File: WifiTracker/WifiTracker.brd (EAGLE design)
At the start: 86.3 x 44.1 mm, 23 parts, among them Y1 16MHz

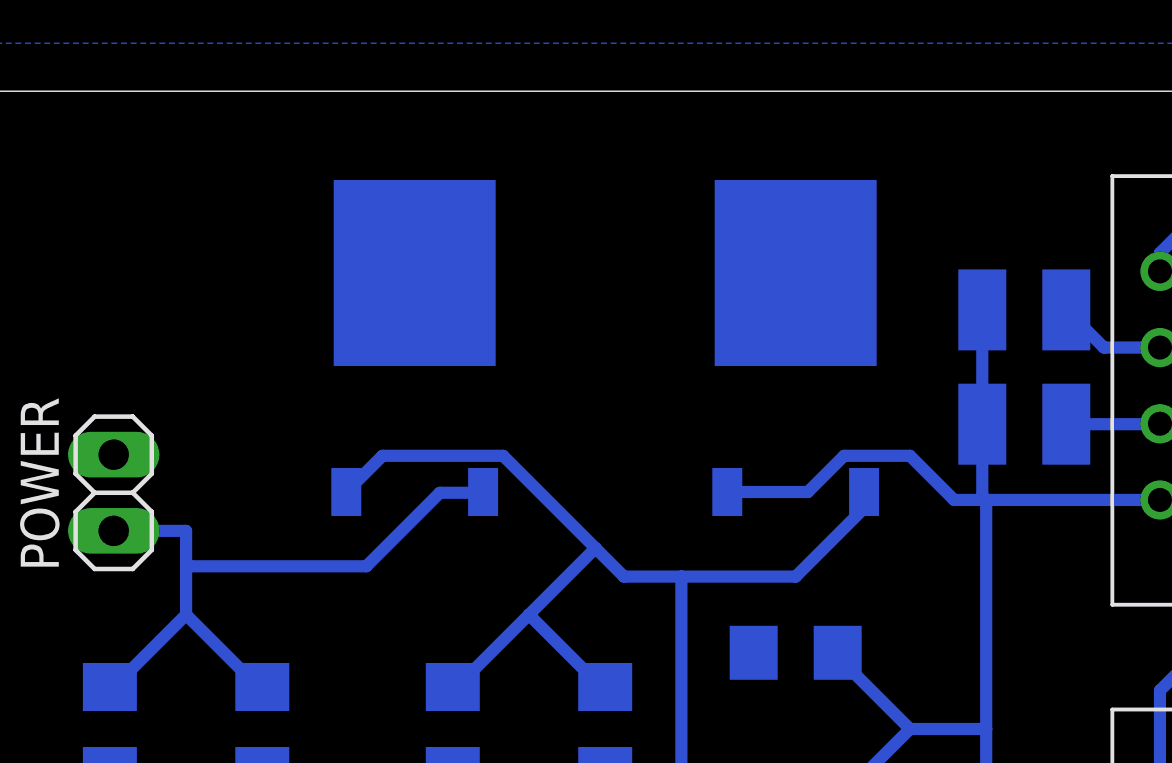
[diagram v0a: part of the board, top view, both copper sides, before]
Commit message: Change generic voltage regulator with specific one
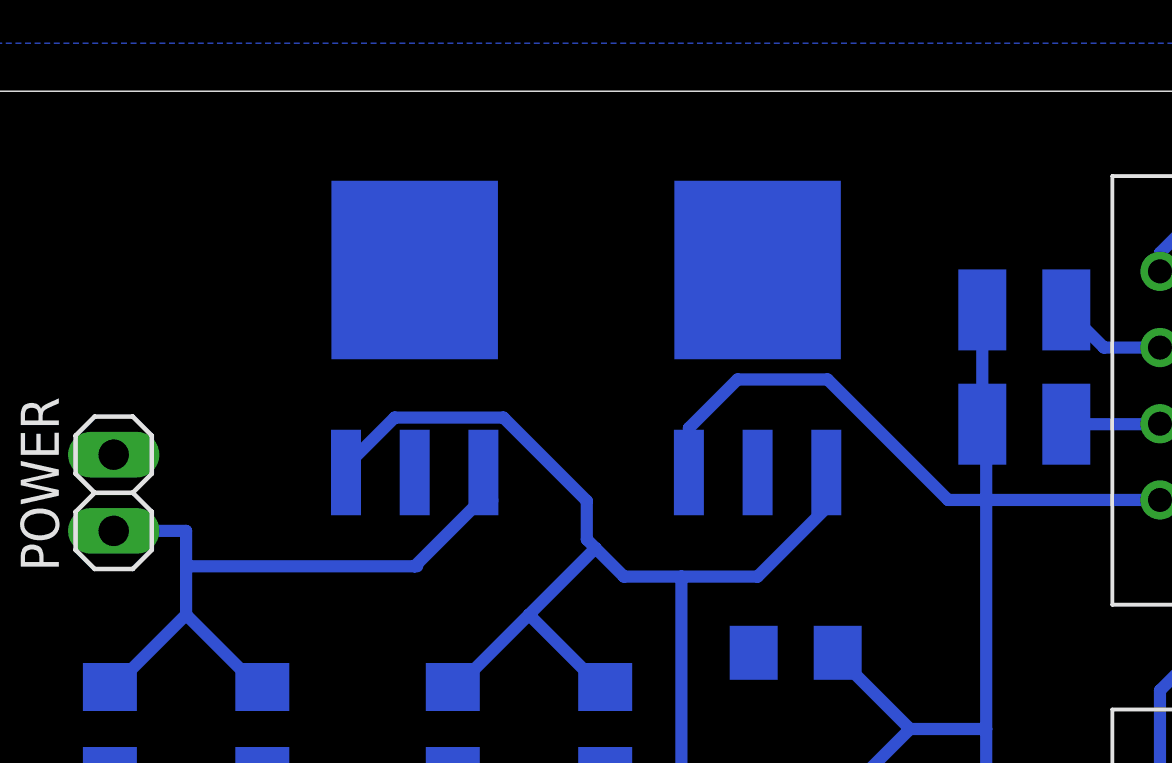
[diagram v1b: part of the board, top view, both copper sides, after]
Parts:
- 3V_REG, 5V_REG: value 7808DT -> LP2950CDT-5.0G; device linear:TO252 -> LP2950CDT-5.0G:TO229P990X238-4N
- moved 3V_REG 1.27 mm to (26.7, 35.6), turned to 90 degrees
- turned 5V_REG to 90 degrees
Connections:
- net 3VCC: now also 3V_REG.3; no longer 3V_REG.2
- net 5VCC: now also 5V_REG.3; no longer 5V_REG.2
- net GND: now also 3V_REG.2, 3V_REG.4, 5V_REG.2, 5V_REG.4; no longer 3V_REG.3, 5V_REG.3
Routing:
- net 3VCC: track 58.5 -> 62.5 mm
- net 5VCC: track 131.6 -> 132.6 mm

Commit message: fix
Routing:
- net 5VCC: track 132.6 -> 135.2 mm
- net VIN: track 23.4 -> 25.9 mm
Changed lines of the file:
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@@
 <wire x1="77.2892" y1="6.4008" x2="77.34" y2="6.35" width="0.4064" layer="16"/>
 <contactref element="5V_REG" pad="3"/>
-<wire x1="18.1983375" y1="33.2414" x2="20.9764" y2="30.4633375" width="0.4064" layer="16"/>
-<wire x1="20.9764" y1="30.4633375" x2="20.9764" y2="29.1783375" width="0.4064" layer="16"/>
-<wire x1="18.1983375" y1="33.2414" x2="14.5716625" y2="33.2414" width="0.4064" layer="16"/>
+<wire x1="18.1983375" y1="34.5114" x2="20.9764" y2="31.7333375" width="0.4064" layer="16"/>
+<wire x1="20.9764" y1="31.7333375" x2="20.9764" y2="29.1783375" width="0.4064" layer="16"/>
+<wire x1="18.1983375" y1="34.5114" x2="14.5716625" y2="34.5114" width="0.4064" layer="16"/>
 <wire x1="20.9764" y1="29.1783375" x2="21.26736875" y2="28.88736875" width="0.4064" layer="16"/>
-<wire x1="14.5716625" y1="33.2414" x2="12.95" y2="31.6197375" width="0.4064" layer="16"/>
-<wire x1="12.95" y1="31.6197375" x2="12.95" y2="31.41" width="0.4064" layer="16"/>
+<wire x1="14.5716625" y1="34.5114" x2="12.95" y2="32.8897375" width="0.4064" layer="16"/>
+<wire x1="12.95" y1="32.8897375" x2="12.95" y2="31.41" width="0.4064" layer="16"/>
 <contactref element="3V_REG" pad="1"/>
 <wire x1="28.96" y1="31.41" x2="28.96" y2="30.23" width="0.4064" layer="16"/>
@@
 <contactref element="C7" pad="1"/>
 <contactref element="C4" pad="1"/>
-<wire x1="7.62" y1="28.2836" x2="15.24" y2="28.2836" width="0.4064" layer="16"/>
-<wire x1="15.24" y1="28.2836" x2="15.3236" y2="28.2836" width="0.4064" layer="16"/>
 <wire x1="5.207" y1="29.464" x2="7.62" y2="29.464" width="0.4064" layer="16"/>
-<wire x1="7.62" y1="29.464" x2="7.62" y2="28.2836" width="0.4064" layer="16"/>
-<wire x1="7.62" y1="28.2836" x2="7.62" y2="26.67" width="0.4064" layer="16"/>
+<wire x1="7.62" y1="29.464" x2="7.62" y2="26.67" width="0.4064" layer="16"/>
 <wire x1="7.62" y1="26.67" x2="5.21" y2="24.26" width="0.4064" layer="16"/>
 <wire x1="5.21" y1="24.26" x2="5.08" y2="24.26" width="0.4064" layer="16"/>
@@
 <wire x1="10.03" y1="24.26" x2="10.16" y2="24.26" width="0.4064" layer="16"/>
 <contactref element="5V_REG" pad="1"/>
-<wire x1="17.4364" y1="30.48" x2="17.78" y2="30.48" width="0.508" layer="16"/>
-<wire x1="15.24" y1="28.2836" x2="17.4364" y2="30.48" width="0.4064" layer="16"/>
-<wire x1="17.4364" y1="30.48" x2="17.53" y2="31.41" width="0" layer="19" extent="16-16"/>
+<wire x1="17.53" y1="31.41" x2="17.78" y2="31.16" width="0.4064" layer="16"/>
+<wire x1="17.78" y1="31.16" x2="17.78" y2="29.21" width="0.4064" layer="16"/>
+<wire x1="17.78" y1="29.21" x2="16.51" y2="27.94" width="0.4064" layer="16"/>
+<wire x1="16.51" y1="27.94" x2="9.144" y2="27.94" width="0.4064" layer="16"/>
+<wire x1="9.144" y1="27.94" x2="7.62" y2="29.464" width="0.4064" layer="16"/>
 </signal>
 <signal name="STA_CH_PD">

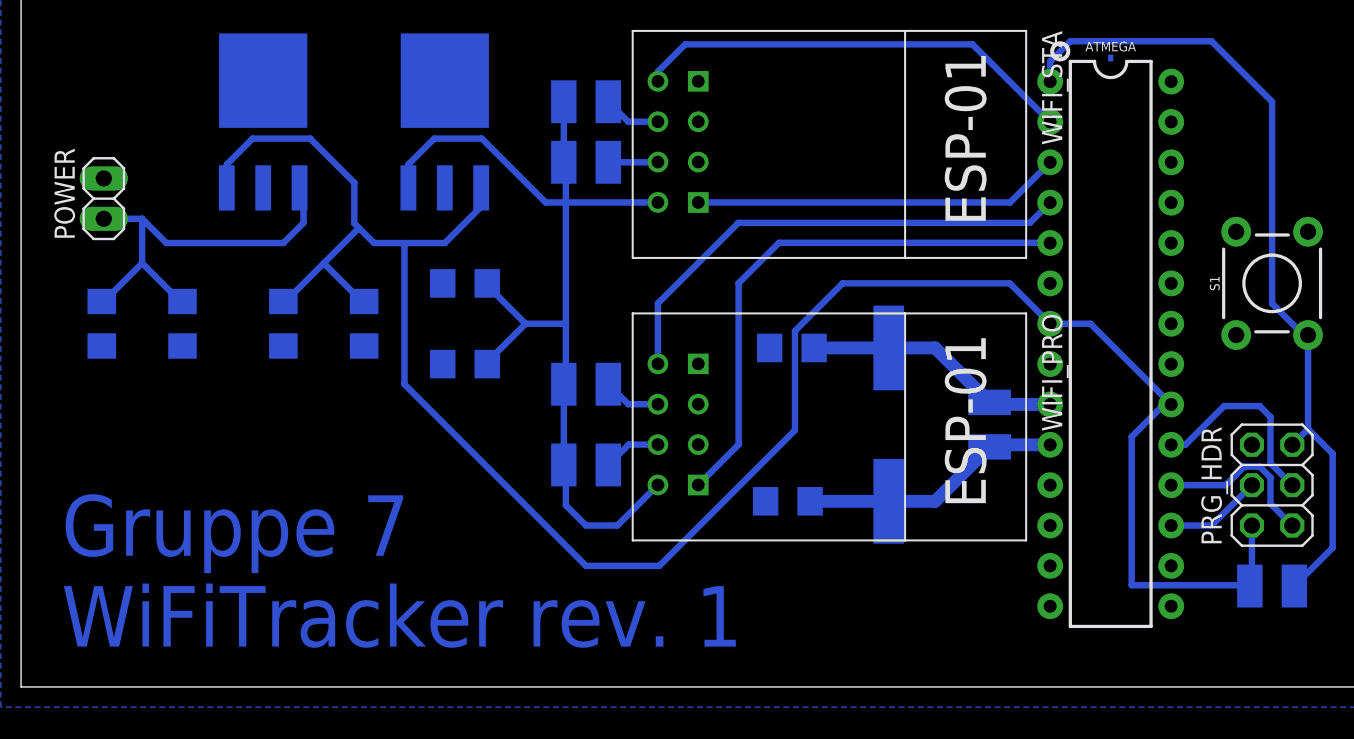
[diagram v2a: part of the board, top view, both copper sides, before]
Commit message: Add power net class and added width
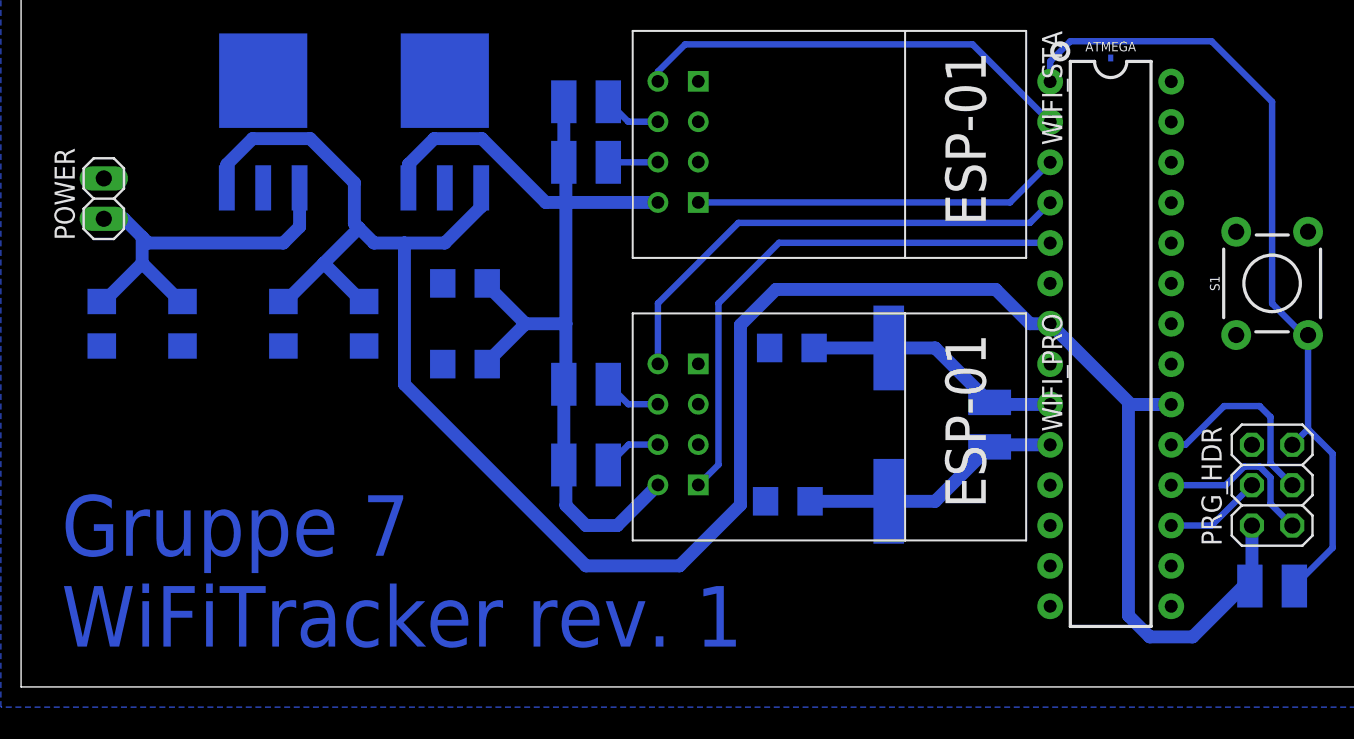
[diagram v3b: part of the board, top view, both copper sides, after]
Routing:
- net 5VCC: track 135.2 -> 143.2 mm
- net VIN: track 25.9 -> 24.6 mm

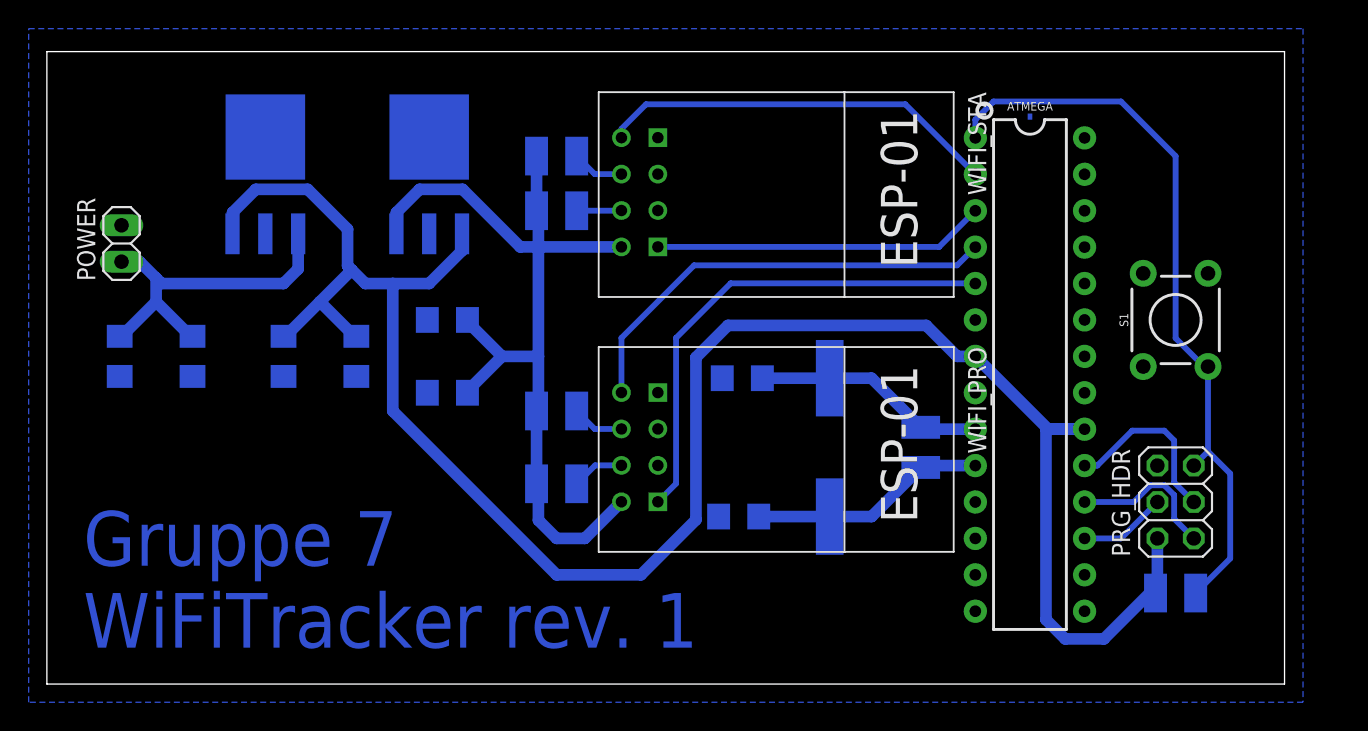
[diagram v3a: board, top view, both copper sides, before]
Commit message: Add power input text
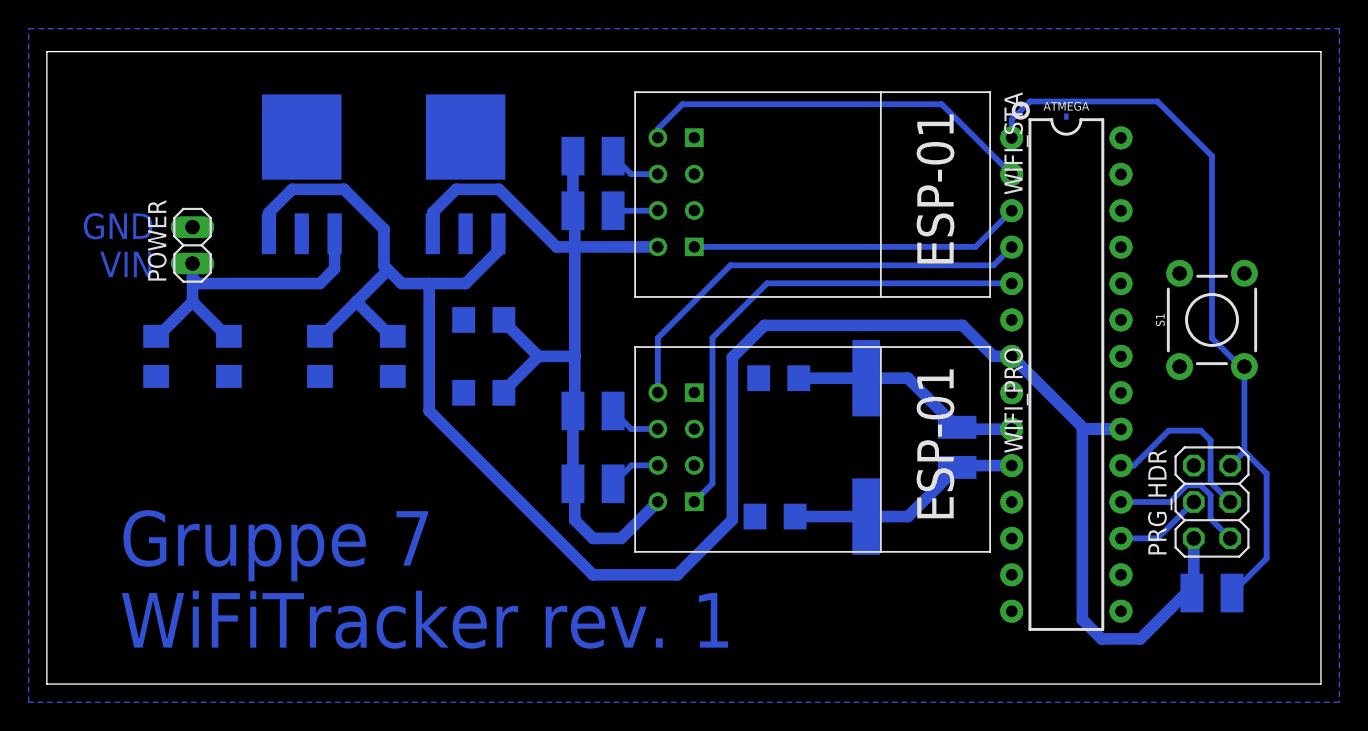
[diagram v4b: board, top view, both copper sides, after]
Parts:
- moved POWER 4.95 mm to (10.2, 30.6)
- moved ATMEGA 2.54 mm to (71.1, 21.6)
- moved PRG_HDR 2.54 mm to (81.3, 12.7)
- moved R6 2.54 mm to (81.3, 6.35)
- moved S1 2.54 mm to (81.3, 25.4)
- moved 5V_REG 2.54 mm to (17.8, 35.6)
- moved C4 2.54 mm to (7.62, 22.9)
- moved 3V_REG 2.54 mm to (29.2, 35.6)
- moved C1 2.54 mm to (51.1, 21.3)
- moved C2 2.54 mm to (50.8, 11.7)
- moved C5 2.54 mm to (24.1, 22.9)
- moved C6 2.54 mm to (30.5, 20.3)
- moved C7 2.54 mm to (12.7, 22.9)
- moved C8 2.54 mm to (19.1, 22.9)
- moved C9 2.54 mm to (30.5, 25.4)
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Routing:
- net VIN: track 24.6 -> 22.7 mm
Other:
- board size 86.3 x 44.1 mm -> 88.9 x 44.1 mm
- board text added: "GND VIN"

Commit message: WifiTracker just got smaller
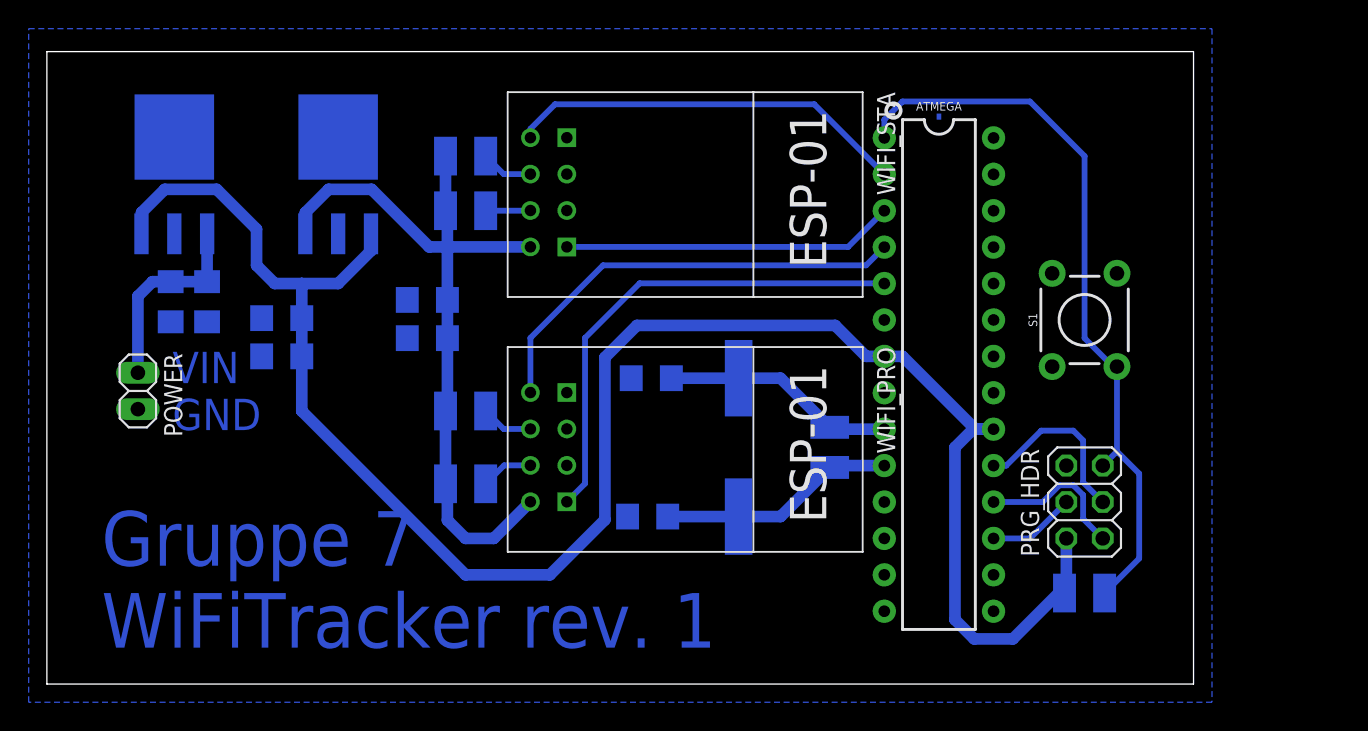
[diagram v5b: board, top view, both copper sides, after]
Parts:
- moved POWER 10.9 mm to (6.35, 20.4), turned to 270 degrees
- moved ATMEGA 8.89 mm to (62.2, 21.6)
- moved 3V_REG 8.89 mm to (20.3, 35.6)
- moved 5V_REG 8.89 mm to (8.89, 35.6)
- moved C1 8.89 mm to (42.2, 21.3)
- moved C2 8.89 mm to (41.9, 11.7)
- moved PRG_HDR 8.89 mm to (72.4, 12.7)
- moved R1 8.89 mm to (29.2, 36.8)
- moved R2 8.89 mm to (29.2, 33.0)
- moved R3 8.89 mm to (29.2, 19.1)
- moved R4 8.89 mm to (54.6, 16.5)
- moved R5 8.89 mm to (29.2, 14.0)
- moved R6 8.89 mm to (72.4, 6.35)
- moved S1 8.89 mm to (72.4, 25.4)
- moved WIFI_PRO 8.89 mm to (41.9, 16.5)
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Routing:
- net 5VCC: track 143.2 -> 131.8 mm
- net 3VCC: track 62.5 -> 52.5 mm
- net VIN: track 22.7 -> 13.9 mm
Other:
- board size 88.9 x 44.1 mm -> 80 x 44.1 mm
- board text added: "VIN GND"
- board text removed: "GND VIN"
